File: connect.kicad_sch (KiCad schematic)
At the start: 37 parts, among them J101 Cortex_Debug, J102 DX07S016JA3, SW101 SKSG, SW102 SKSG, SW103 SKSG, SW104 SKSG, SW105 SKSG, U101 TPS78433QWDRBRQ1, U102 ATSAMD51J, Y101 32k768

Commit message: Update library
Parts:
- J101: value Cortex_Debug -> Cortex; footprint V2_Cortex_Debug:Cortex_Debug_Pad -> V2_Connector_Debug:Cortex; symbol V2_Cortex_Debug:Cortex_Debug -> V2_Connector_Debug:Cortex
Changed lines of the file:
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@@
 	)
 	(symbol
-		(lib_id "V2_Cortex_Debug:Cortex_Debug")
+		(lib_id "V2_Connector_Debug:Cortex")
 		(at 123.19 99.06 0)
 		(unit 1)
@@
 			)
 		)
-		(property "Value" "Cortex_Debug"
+		(property "Value" "Cortex"
 			(at 124.46 88.9 0)
 			(effects
@@
 			)
 		)
-		(property "Footprint" "V2_Cortex_Debug:Cortex_Debug_Pad"
+		(property "Footprint" "V2_Connector_Debug:Cortex"
 			(at 123.19 113.03 0)
 			(effects
@@
 		(at 171.45 154.94 0)
 		(unit 1)
-		(exclude_from_sim yes)
+		(exclude_from_sim no)
 		(in_bom no)
 		(on_board yes)
@@
 			(at 171.45 154.94 0)
 			(effects
+				(font
+					(size 1.27 1.27)
+				)
+				(hide yes)
+			)
+		)
+		(property "Sim.Enable" "0"
+			(at 171.45 154.94 0)
+			(effects

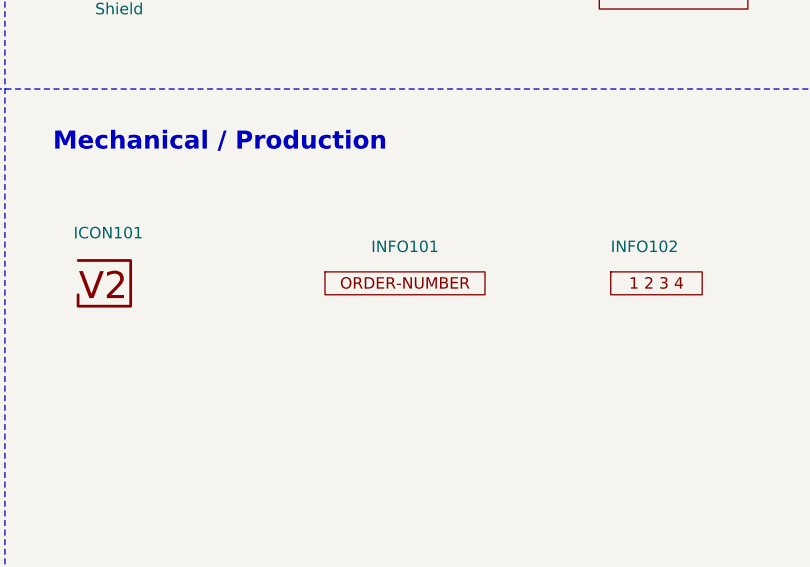
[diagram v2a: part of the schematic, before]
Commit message: Replace Order_Number
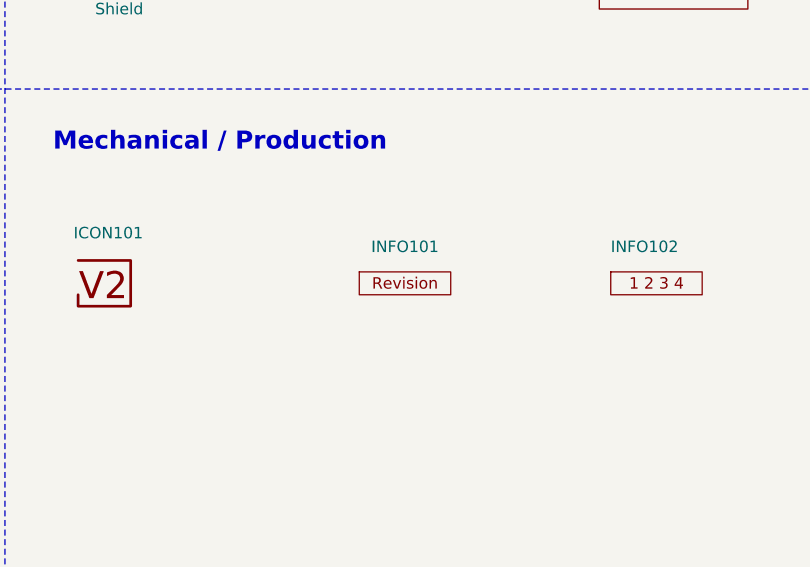
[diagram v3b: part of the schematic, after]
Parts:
- INFO101: value Order_Number -> ~; footprint V2_Production:Order_Number -> V2_Production:Revision; symbol V2_Production:Order_Number -> V2_Production:Revision
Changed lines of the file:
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@@
 	(title_block
 		(title "V2 connect")
-		(date "2026-02-10")
-		(rev "2026-02-10")
+		(date "2026-02-12")
+		(rev "2026-02-12")
 		(company "Versio Duo")
 	)
@@
 	)
 	(symbol
-		(lib_id "V2_Production:Order_Number")
+		(lib_id "V2_Production:Revision")
 		(at 204.47 154.94 0)
 		(unit 1)
@@
 			)
 		)
-		(property "Value" "Order_Number"
+		(property "Value" "~"
 			(at 204.47 157.48 0)
 			(effects
@@
 			)
 		)
-		(property "Footprint" "V2_Production:Order_Number"
+		(property "Footprint" "V2_Production:Revision"
 			(at 204.47 160.02 0)
 			(effects
@@
 		(at 171.45 154.94 0)
 		(unit 1)
-		(exclude_from_sim yes)
+		(exclude_from_sim no)
 		(in_bom no)
 		(on_board yes)
